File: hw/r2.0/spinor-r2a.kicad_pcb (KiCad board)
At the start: 4 copper layers, 50 x 63.5 mm, 150 parts, among them J9 Conn_01x05, Q1 NMOS, Q2 NMOS, Q3 NMOS, Q4 NMOS, Q5 NMOS, Q6 NMOS, U1 TCAN334G, U2 STM32G474CETx, U3 AS5047D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

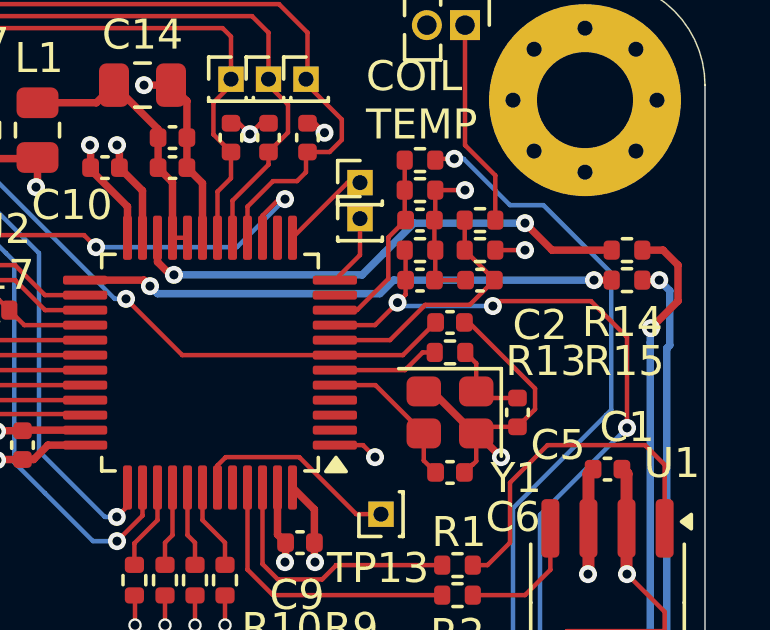
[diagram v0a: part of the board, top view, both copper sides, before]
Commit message: archive c++ firmware
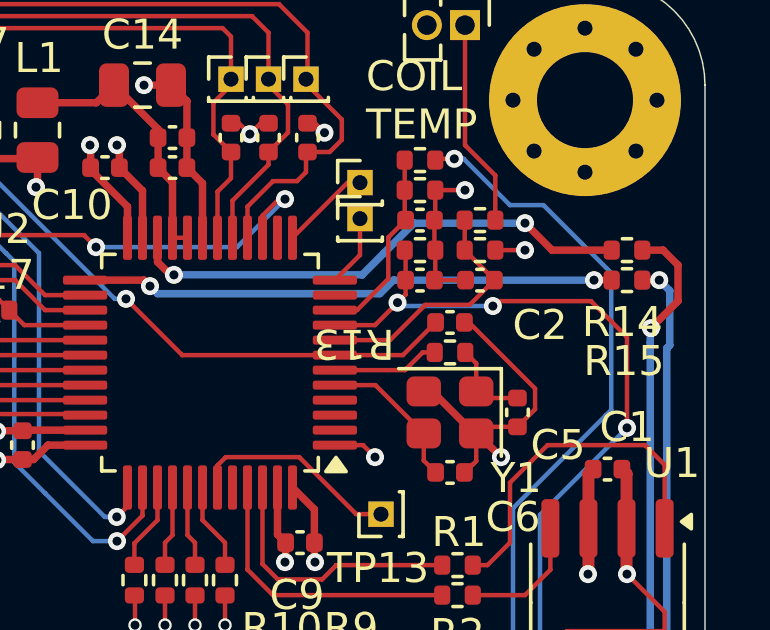
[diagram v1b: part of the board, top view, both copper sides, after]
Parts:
- turned R13 to 0 degrees
- turned R32 to 0 degrees
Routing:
- net VDD: track 106.7 -> 105.7 mm, vias 23 -> 22
- net /Microcontroller/ADC12_IN1: track 8.56 -> 9.55 mm, vias 0 -> 1
